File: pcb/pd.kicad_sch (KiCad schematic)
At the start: 28 parts, among them J1 Conn_01x02, SW1 SW_SPST, U1 BQ27220, U2 TPS630252, U3 PCA9410AUKZ, U4 HX4054A, U5 SGM6602-12

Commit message: chore: added one (1) todo
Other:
- note added: "TODO: TVS Diode somewhere?"
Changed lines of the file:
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@@
+		)
+	)
+	(text "TODO: TVS Diode somewhere?"
+		(exclude_from_sim no)
+		(at 169.164 154.432 0)
+		(effects
+			(font
+				(size 1.27 1.27)
+				(italic yes)
+				(color 255 0 255 1)
+			)
 		)
 	)

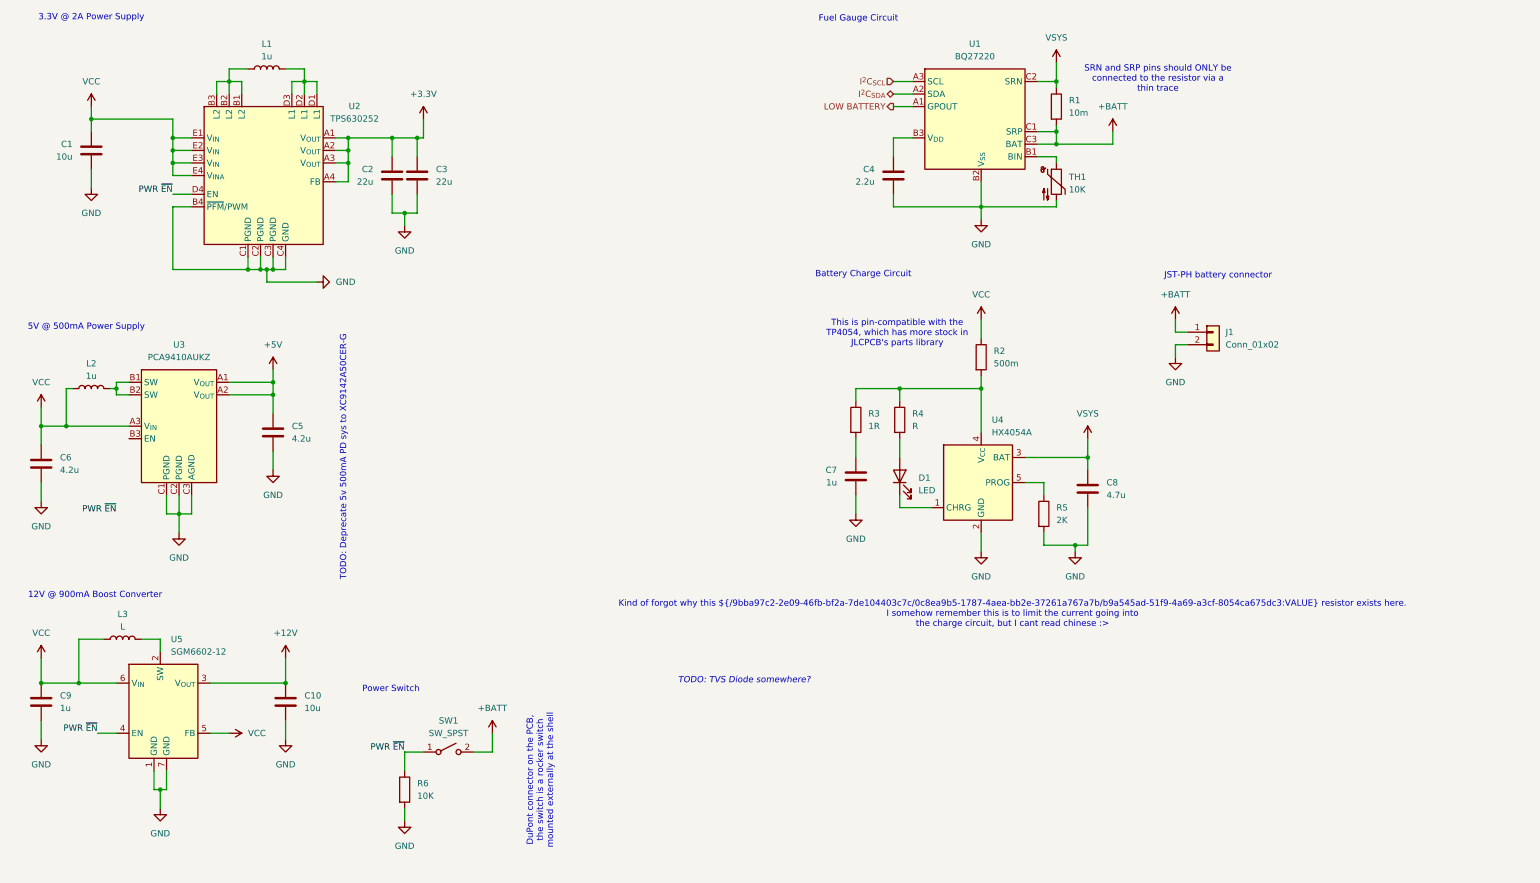
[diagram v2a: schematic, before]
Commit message: feat: changed 5v boost controller
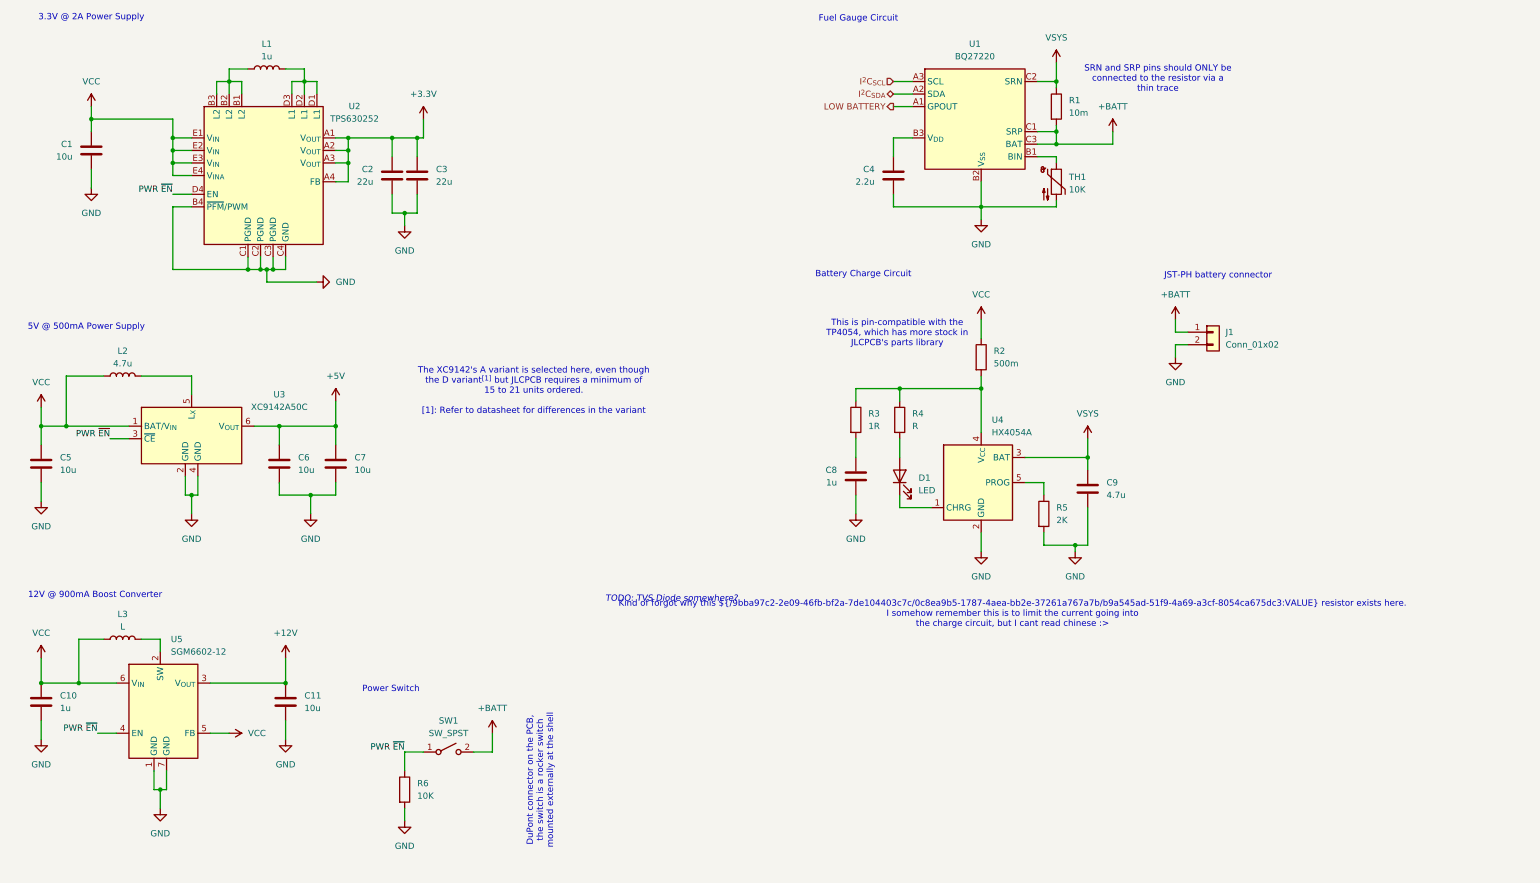
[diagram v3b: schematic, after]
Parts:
- removed U3: PCA9410AUKZ, Banshee:WLCSP9_1P24X1P24_NXP, symbol Banshee:PCA9410AUKZ
- added C7: 10u, symbol Device:C
- added U3: XC9142A50C, Banshee:XC9142A50CERG, symbol Banshee:XC9142
- C5: renamed from C6; value 4.2u -> 10u
- C6: renamed from C5; value 4.2u -> 10u
- L2: value 1u -> 4.7u
- renumbered C9 to C10, C10 to C11, C7 to C8, C8 to C9
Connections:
- net +5V: now also C7.2, U3.6 (V_{OUT})
- net GND: now also C7.1, U3.2 (GND), U3.4 (GND)
- net PWR ~{EN}: now also U3.3 (~{CE})
- net VCC: now also U3.1 (BAT/V_{IN})
- net at L2.2: now also U3.5 (L_{X})
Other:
- note added: "The XC9142's A variant is selected here, even though the D variant^{[1]} but JLCPCB requires a minimum of 15 to 21 units ordered. [1]: Refer to datasheet for differences in the variant"
- note removed: "TODO: Deprecate 5v 500mA PD sys to XC9142A50CER-G"
- moved on the sheet: C6, L2
